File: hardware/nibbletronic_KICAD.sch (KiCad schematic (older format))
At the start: 16 parts, among them P1 DIN_5, SW1 SWITCH_INV, SW2 SWITCH_INV, SW3 SWITCH_INV, SW4 SWITCH_INV, SW5 SWITCH_INV, SW6 SW_PUSH, U1 Arduino_micro, U2 MPX5010DP, U3 Joystick

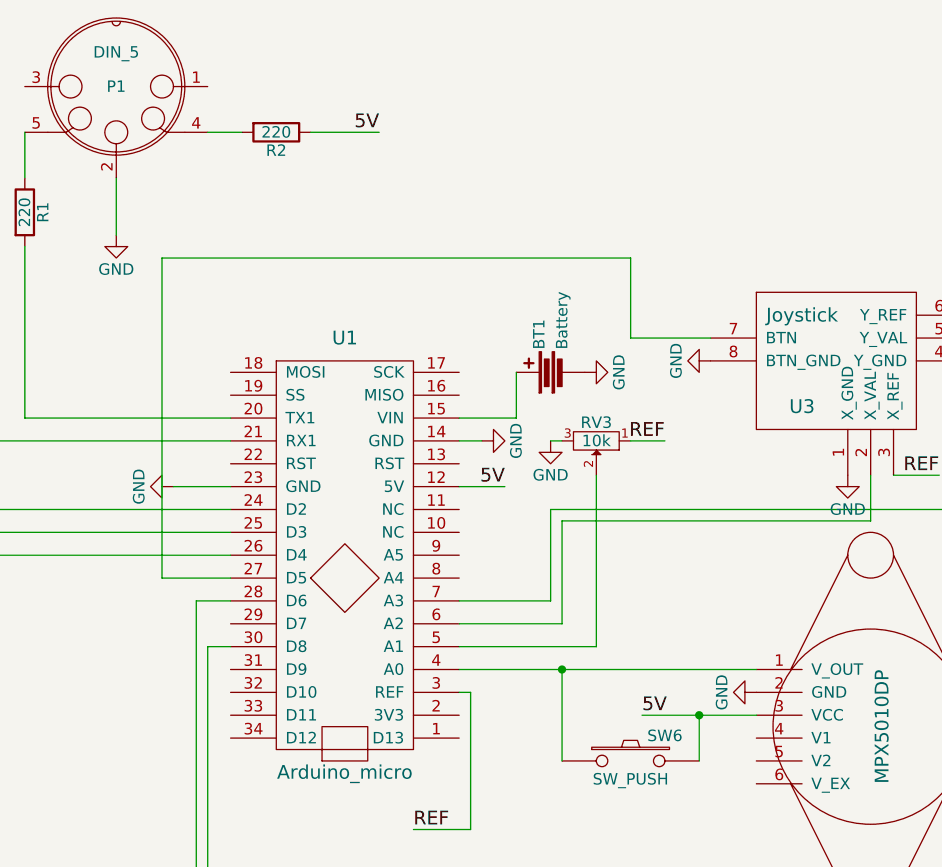
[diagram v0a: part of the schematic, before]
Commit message: Changed footprints for slider, joystick and mode selector switch, added diode and power switch
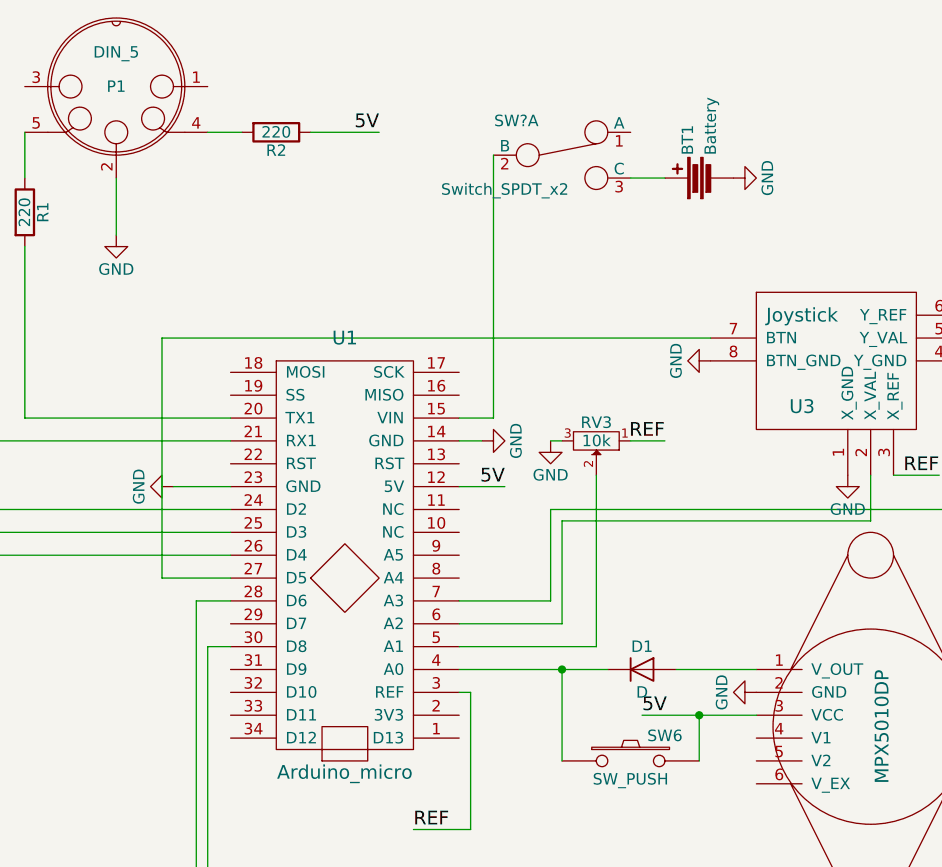
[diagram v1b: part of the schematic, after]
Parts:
- added D1: D, Diodes_ThroughHole:Diode_DO-35_SOD27_Horizontal_RM10, symbol D
- added SW?: Switch_SPDT_x2, symbol Switch_SPDT_x2
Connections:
- net at U1.15 (VIN): now also SW?.2 (B); no longer BT1.1
- net at SW6.1, U1.4 (A0): now also D1.1 (K); no longer U2.1 (V_OUT)
- new net: D1.2 (A), U2.1 (V_OUT)
- new net: BT1.1, SW?.3 (C)
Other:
- moved on the sheet: BT1
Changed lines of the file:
@@
 L Battery BT1
 U 1 1 577E5E4D
-P 5500 2300
-F 0 "BT1" H 5600 2350 50  0000 L CNN
-F 1 "Battery" H 5600 2250 50  0000 L CNN
-F 2 "CustomParts:9V_BATTERY_CLIP" V 5500 2340 50  0001 C CNN
-F 3 "" V 5500 2340 50  0000 C CNN
-	1    5500 2300
+P 6150 1450
+F 0 "BT1" H 6250 1500 50  0000 L CNN
+F 1 "Battery" H 6250 1400 50  0000 L CNN
+F 2 "CustomParts:9V_BATTERY_CLIP" V 6150 1490 50  0001 C CNN
+F 3 "" V 6150 1490 50  0000 C CNN
+	1    6150 1450
 	0    -1   -1   0
 $EndComp
@@
 L GND #PWR02
 U 1 1 577E6679
-P 5650 2300
-F 0 "#PWR02" H 5650 2050 50  0001 C CNN
-F 1 "GND" H 5650 2150 50  0000 C CNN
-F 2 "" H 5650 2300 50  0000 C CNN
-F 3 "" H 5650 2300 50  0000 C CNN
-	1    5650 2300
+P 6300 1450
+F 0 "#PWR02" H 6300 1200 50  0001 C CNN
+F 1 "GND" H 6300 1300 50  0000 C CNN
+F 2 "" H 6300 1450 50  0000 C CNN
+F 3 "" H 6300 1450 50  0000 C CNN
+	1    6300 1450
 	0    -1   -1   0
 $EndComp
@@
 	2600 3750 2400 3750
 Wire Wire Line
-	5100 3600 6400 3600
-Wire Wire Line
 	3200 1250 3200 1450
 Wire Wire Line
@@
 	4450 1250 4750 1250
 Wire Wire Line
-	5100 2500 5350 2500
-Wire Wire Line
-	5350 2500 5350 2300
-Wire Wire Line
 	2750 2900 4100 2900
 Wire Wire Line
 	4100 3300 3950 3300
 Wire Wire Line
-	6200 2150 5850 2150
-Wire Wire Line
-	5850 2150 5850 1800
-Wire Wire Line
-	5850 1800 3800 1800
-Wire Wire Line
-	3800 1800 3800 3200
-Wire Wire Line
 	3800 3200 4100 3200
 Wire Wire Line
 	5550 4000 5550 3600
+$Comp
+L D D1
+U 1 1 578E172C
+P 5900 3600
+F 0 "D1" H 5900 3700 50  0000 C CNN
+F 1 "D" H 5900 3500 50  0000 C CNN
+F 2 "Diodes_ThroughHole:Diode_DO-35_SOD27_Horizontal_RM10" H 5900 3600 50  0001 C CNN
+F 3 "" H 5900 3600 50  0000 C CNN
+	1    5900 3600
+	1    0    0    -1
+$EndComp
+Wire Wire Line
+	6400 3600 6050 3600
+Wire Wire Line
+	5100 3600 5750 3600
+$Comp
+L Switch_SPDT_x2 SW?
+U 1 1 57F7F6C6
+P 5550 1350
+F 0 "SW?" H 5350 1500 50  0000 C CNN
+F 1 "Switch_SPDT_x2" H 5300 1200 50  0000 C CNN
+F 2 "" H 5550 1350 50  0000 C CNN
+F 3 "" H 5550 1350 50  0000 C CNN
+	1    5550 1350
+	1    0    0    -1
+$EndComp
+Wire Wire Line
+	6000 1450 5850 1450
+Wire Wire Line
+	5250 1350 5250 2500
+Wire Wire Line
+	5250 2500 5100 2500
+Wire Wire Line
+	3800 3200 3800 2150
+Wire Wire Line
+	3800 2150 6200 2150
 $EndSCHEMATC

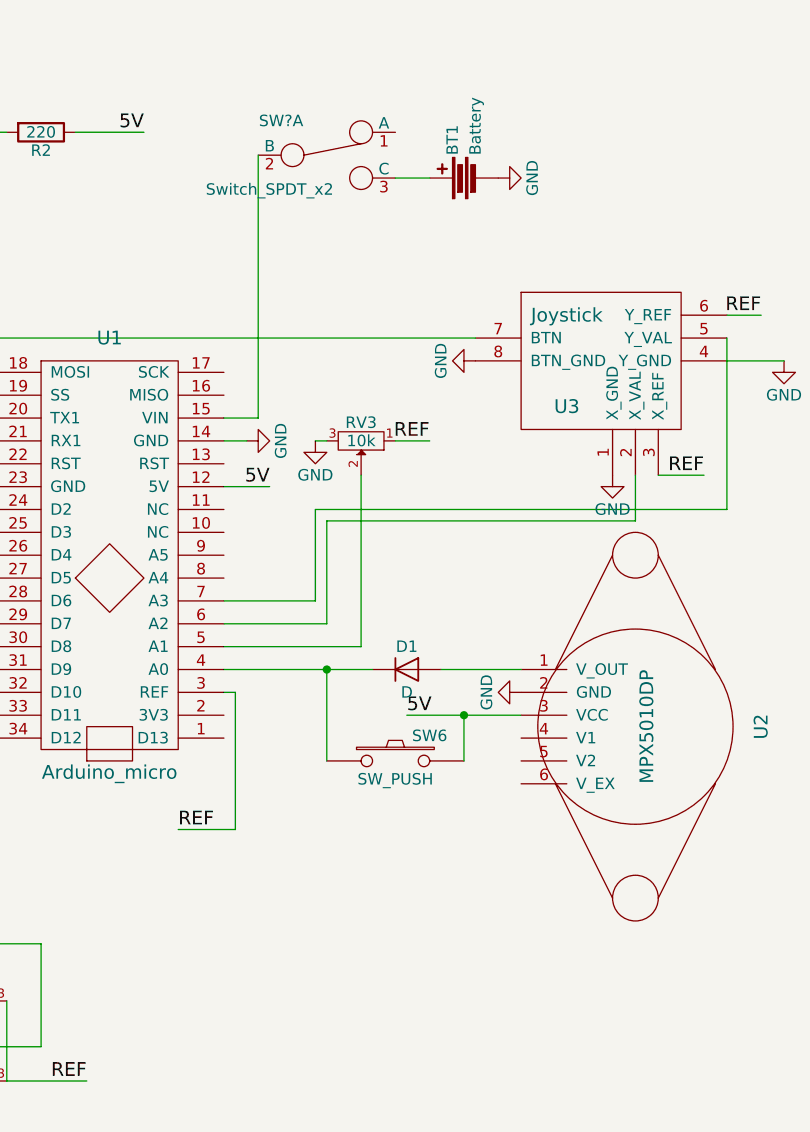
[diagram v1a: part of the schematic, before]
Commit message: Changed PCBlayout, added new footprints, changed spacing, switched to SMD diode, resistors, buttons and switches.
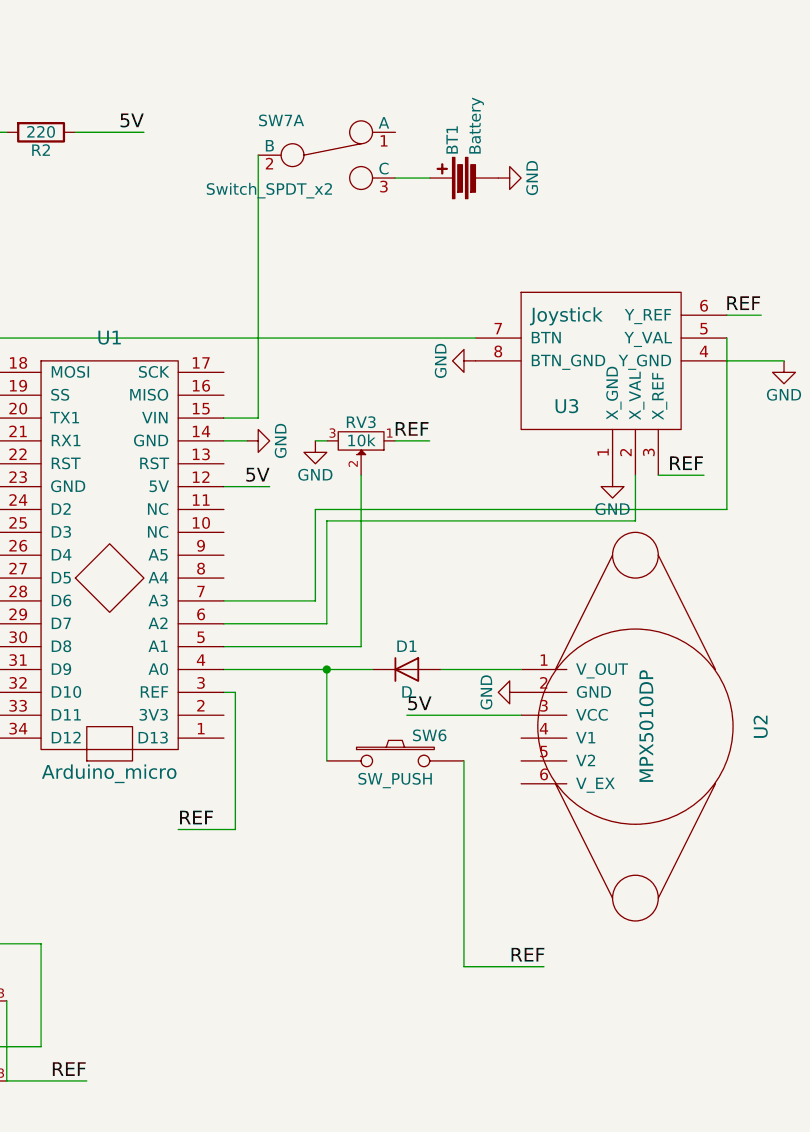
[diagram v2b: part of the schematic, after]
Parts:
- D1: footprint Diodes_ThroughHole:Diode_DO-35_SOD27_Horizontal_RM10 -> Diodes_SMD:D_0805
- R1, R2: footprint Resistors_ThroughHole:Resistor_Horizontal_RM10mm -> Resistors_SMD:R_0805_HandSoldering
- SW5: footprint CustomParts:YSS_1203 -> Buttons_Switches_SMD:SW_SPDT_PCM12
- SW6: footprint Buttons_Switches_ThroughHole:SW_PUSH_SMALL -> Buttons_Switches_SMD:SW_SPST_B3S-1000
- SW7: renamed from SW?; footprint (none) -> Buttons_Switches_SMD:SW_SPDT_PCM12
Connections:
- net 5V: no longer SW6.2
- net REF: now also SW6.2
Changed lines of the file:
@@
 F 0 "R2" V 4380 1250 50  0000 C CNN
 F 1 "220" V 4300 1250 50  0000 C CNN
-F 2 "Resistors_ThroughHole:Resistor_Horizontal_RM10mm" V 4230 1250 50  0001 C CNN
+F 2 "Resistors_SMD:R_0805_HandSoldering" V 4230 1250 50  0001 C CNN
 F 3 "" H 4300 1250 50  0000 C CNN
 	1    4300 1250
@@
 F 0 "R1" V 3280 1600 50  0000 C CNN
 F 1 "220" V 3200 1600 50  0000 C CNN
-F 2 "Resistors_ThroughHole:Resistor_Horizontal_RM10mm" V 3130 1600 50  0001 C CNN
+F 2 "Resistors_SMD:R_0805_HandSoldering" V 3130 1600 50  0001 C CNN
 F 3 "" H 3200 1600 50  0000 C CNN
 	1    3200 1600
@@
 F 0 "SW5" H 2950 4800 50  0000 C CNN
 F 1 "SWITCH_INV" H 3000 4500 50  0000 C CNN
-F 2 "CustomParts:YSS_1203" H 3150 4650 50  0001 C CNN
+F 2 "Buttons_Switches_SMD:SW_SPDT_PCM12" H 3150 4650 50  0001 C CNN
 F 3 "" H 3150 4650 50  0000 C CNN
 	1    3150 4650
@@
 F 0 "SW6" H 6000 4110 50  0000 C CNN
 F 1 "SW_PUSH" H 5850 3920 50  0000 C CNN
-F 2 "Buttons_Switches_ThroughHole:SW_PUSH_SMALL" H 5850 4000 50  0001 C CNN
+F 2 "Buttons_Switches_SMD:SW_SPST_B3S-1000" H 5850 4000 50  0001 C CNN
 F 3 "" H 5850 4000 50  0000 C CNN
 	1    5850 4000
@@
 Wire Wire Line
 	5900 3800 6400 3800
-Wire Wire Line
-	6150 4000 6150 3800
-Connection ~ 6150 3800
 Connection ~ 5550 3600
 Wire Wire Line
@@
 F 0 "D1" H 5900 3700 50  0000 C CNN
 F 1 "D" H 5900 3500 50  0000 C CNN
-F 2 "Diodes_ThroughHole:Diode_DO-35_SOD27_Horizontal_RM10" H 5900 3600 50  0001 C CNN
+F 2 "Diodes_SMD:D_0805" H 5900 3600 50  0001 C CNN
 F 3 "" H 5900 3600 50  0000 C CNN
 	1    5900 3600
@@
 	5100 3600 5750 3600
 $Comp
-L Switch_SPDT_x2 SW?
+L Switch_SPDT_x2 SW7
 U 1 1 57F7F6C6
 P 5550 1350
-F 0 "SW?" H 5350 1500 50  0000 C CNN
+F 0 "SW7" H 5350 1500 50  0000 C CNN
 F 1 "Switch_SPDT_x2" H 5300 1200 50  0000 C CNN
-F 2 "" H 5550 1350 50  0000 C CNN
+F 2 "Buttons_Switches_SMD:SW_SPDT_PCM12" H 5550 1350 50  0001 C CNN
 F 3 "" H 5550 1350 50  0000 C CNN
 	1    5550 1350
@@
 Wire Wire Line
 	3800 2150 6200 2150
+Wire Wire Line
+	6150 4000 6150 4900
+Wire Wire Line
+	6150 4900 6500 4900
+Text Label 6350 4900 0    60   ~ 0
+REF
 $EndSCHEMATC

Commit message: Changed switches and button due to parts availability, updated BOM
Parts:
- SW5, SW7: footprint Buttons_Switches_SMD:SW_SPDT_PCM12 -> CustomParts:ESP40XX
- SW6: footprint Buttons_Switches_SMD:SW_SPST_B3S-1000 -> CustomParts:SMD_Pushbutton
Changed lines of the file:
@@
 F 0 "SW5" H 2950 4800 50  0000 C CNN
 F 1 "SWITCH_INV" H 3000 4500 50  0000 C CNN
-F 2 "Buttons_Switches_SMD:SW_SPDT_PCM12" H 3150 4650 50  0001 C CNN
+F 2 "CustomParts:ESP40XX" H 3150 4650 50  0001 C CNN
 F 3 "" H 3150 4650 50  0000 C CNN
 	1    3150 4650
@@
 F 0 "SW6" H 6000 4110 50  0000 C CNN
 F 1 "SW_PUSH" H 5850 3920 50  0000 C CNN
-F 2 "Buttons_Switches_SMD:SW_SPST_B3S-1000" H 5850 4000 50  0001 C CNN
+F 2 "CustomParts:SMD_Pushbutton" H 5850 4000 50  0001 C CNN
 F 3 "" H 5850 4000 50  0000 C CNN
 	1    5850 4000
@@
 F 0 "SW7" H 5350 1500 50  0000 C CNN
 F 1 "Switch_SPDT_x2" H 5300 1200 50  0000 C CNN
-F 2 "Buttons_Switches_SMD:SW_SPDT_PCM12" H 5550 1350 50  0001 C CNN
+F 2 "CustomParts:ESP40XX" H 5550 1350 50  0001 C CNN
 F 3 "" H 5550 1350 50  0000 C CNN
 	1    5550 1350

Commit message: fixed note interpretation
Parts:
- BT1: symbol Battery -> Battery-RESCUE-nibbletronic_KICAD
- RV1, RV2, RV3: symbol POT -> POT-RESCUE-nibbletronic_KICAD
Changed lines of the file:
@@
 EESchema Schematic File Version 2
+LIBS:nibbletronic_KICAD-rescue
 LIBS:power
 LIBS:device
@@
 $EndComp
 $Comp
-L POT RV3
+L POT-RESCUE-nibbletronic_KICAD RV3
 U 1 1 574F2601
 P 5700 2600
@@
 $EndComp
 $Comp
-L Battery BT1
+L Battery-RESCUE-nibbletronic_KICAD BT1
 U 1 1 577E5E4D
 P 6150 1450
@@
 $EndComp
 $Comp
-L POT RV1
+L POT-RESCUE-nibbletronic_KICAD RV1
 U 1 1 577E60FF
 P 4000 5050
@@
 $EndComp
 $Comp
-L POT RV2
+L POT-RESCUE-nibbletronic_KICAD RV2
 U 1 1 577E6156
 P 4000 5400

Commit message: Beginning Hardware Revision 2.0
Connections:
- net at SW1.2: now also U1.24 (D2); no longer U1.21 (RX1)
- net at SW2.2: now also U1.25 (D3); no longer U1.24 (D2)
- net at SW3.2: now also U1.26 (D4); no longer U1.25 (D3)
- net at SW4.2: now also U1.27 (D5); no longer U1.26 (D4)
- net at U3.7 (BTN): now also U1.28 (D6); no longer U1.27 (D5)
- net at RV1.2: now also U1.8 (A4); no longer U1.28 (D6)
- net at U1.30 (D8): no longer RV2.2
- net at U1.9 (A5): now also RV2.2
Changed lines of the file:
@@
-$EndComp
-$Comp
-L POT-RESCUE-nibbletronic_KICAD RV1
-U 1 1 577E60FF
-P 4000 5050
-F 0 "RV1" H 4000 4970 50  0000 C CNN
-F 1 "10k" H 4000 5050 50  0000 C CNN
-F 2 "CustomParts:ALPS_402125" H 4000 5050 50  0001 C CNN
-F 3 "" H 4000 5050 50  0000 C CNN
-	1    4000 5050
-	1    0    0    -1
 $EndComp
 $Comp
@@
 Connection ~ 2600 3750
 Wire Wire Line
-	3000 2000 3000 2600
+	3000 2000 3000 2900
 Wire Wire Line
 	1400 2000 3000 2000
@@
 	1250 3900 2850 3900
 Wire Wire Line
-	2850 3000 4100 3000
-Wire Wire Line
-	4100 3100 2950 3100
-Wire Wire Line
 	1300 3850 2950 3850
 Wire Wire Line
@@
 Wire Wire Line
 	4000 1250 4150 1250
-Wire Wire Line
-	3000 2600 4100 2600
 Wire Wire Line
 	2400 2150 2500 2150
@@
 	2600 4750 2650 4750
 Wire Wire Line
-	2750 4000 2750 2900
-Wire Wire Line
-	2850 3900 2850 3000
-Wire Wire Line
-	2950 3850 2950 3100
-Wire Wire Line
 	5100 3500 5700 3500
 Wire Wire Line
@@
 	7300 2900 7300 2150
 Wire Wire Line
-	3950 3300 3950 4900
-Wire Wire Line
-	3950 4900 4000 4900
-Wire Wire Line
-	4100 3500 4000 3500
-Wire Wire Line
-	4000 3500 4000 4800
-Wire Wire Line
-	4000 4800 4300 4800
-Wire Wire Line
-	4300 4800 4300 5250
-Wire Wire Line
-	4300 5250 4000 5250
+	4000 5250 5300 5250
 Wire Wire Line
 	5100 2800 5300 2800
@@
 Wire Wire Line
 	4450 1250 4750 1250
-Wire Wire Line
-	2750 2900 4100 2900
-Wire Wire Line
-	4100 3300 3950 3300
-Wire Wire Line
-	3800 3200 4100 3200
 Wire Wire Line
 	5550 4000 5550 3600
@@
 	5250 2500 5100 2500
 Wire Wire Line
-	3800 3200 3800 2150
+	3800 2150 3800 3300
 Wire Wire Line
 	3800 2150 6200 2150
@@
 Text Label 6350 4900 0    60   ~ 0
 REF
+$Comp
+L POT-RESCUE-nibbletronic_KICAD RV1
+U 1 1 577E60FF
+P 4000 5050
+F 0 "RV1" H 4000 4970 50  0000 C CNN
+F 1 "10k" H 4000 5050 50  0000 C CNN
+F 2 "CustomParts:ALPS_402125" H 4000 5050 50  0001 C CNN
+F 3 "" H 4000 5050 50  0000 C CNN
+	1    4000 5050
+	1    0    0    -1
+$EndComp
+Wire Wire Line
+	5100 3200 5250 3200
+Wire Wire Line
+	5250 3200 5250 4900
+Wire Wire Line
+	5250 4900 4000 4900
+Wire Wire Line
+	5100 3100 5300 3100
+Wire Wire Line
+	5300 3100 5300 5250
+Wire Wire Line
+	3000 2900 4100 2900
+Wire Wire Line
+	2750 4000 2750 3000
+Wire Wire Line
+	2750 3000 4100 3000
+Wire Wire Line
+	2850 3900 2850 3100
+Wire Wire Line
+	2850 3100 4100 3100
+Wire Wire Line
+	2950 3850 2950 3200
+Wire Wire Line
+	2950 3200 4100 3200
+Wire Wire Line
+	3800 3300 4100 3300
 $EndSCHEMATC
